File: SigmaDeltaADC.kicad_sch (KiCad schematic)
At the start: 6 parts, among them U5 ADS122C04IPWR

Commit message: Routed most PCB traces
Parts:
- C10, C11: value C -> 0.1u
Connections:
- net 3.3V renamed +3V3
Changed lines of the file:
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@@
     )
   )
-  (symbol (lib_id "SparkFun-PowerSymbols:3.3V") (at 86.868 98.044 0) (unit 1)
-    (in_bom yes) (on_board yes) (fields_autoplaced)
-    (property "Reference" "#SUPPLY01" (id 0) (at 88.138 98.044 0)
-      (effects (font (size 1.143 1.143)) (justify left bottom) hide)
-    )
-    (property "Value" "3.3V" (id 1) (at 88.2651 95.8998 0)
-      (effects (font (size 1.143 1.143)) (justify left))
-    )
-    (property "Footprint" "XXX-00000" (id 2) (at 88.2651 98.8007 0)
-      (effects (font (size 1.524 1.524)) (justify left))
+  (symbol (lib_id "power:+3V3") (at 86.868 98.044 0) (unit 1)
+    (in_bom yes) (on_board yes) (fields_autoplaced)
+    (property "Reference" "#PWR0133" (id 0) (at 86.868 101.854 0)
+      (effects (font (size 1.27 1.27)) hide)
+    )
+    (property "Value" "+3V3" (id 1) (at 86.868 94.4394 0))
+    (property "Footprint" "" (id 2) (at 86.868 98.044 0)
+      (effects (font (size 1.27 1.27)) hide)
     )
     (property "Datasheet" "" (id 3) (at 86.868 98.044 0)
-      (effects (font (size 1.524 1.524)) hide)
-    )
-    (pin "~")
-  )
-  (symbol (lib_id "SparkFun-PowerSymbols:3.3V") (at 113.538 133.096 180) (unit 1)
-    (in_bom yes) (on_board yes) (fields_autoplaced)
-    (property "Reference" "#SUPPLY02" (id 0) (at 112.268 133.096 0)
-      (effects (font (size 1.143 1.143)) (justify left bottom) hide)
-    )
-    (property "Value" "3.3V" (id 1) (at 114.9351 133.1108 0)
-      (effects (font (size 1.143 1.143)) (justify right))
-    )
-    (property "Footprint" "XXX-00000" (id 2) (at 114.9351 136.0117 0)
-      (effects (font (size 1.524 1.524)) (justify right))
+      (effects (font (size 1.27 1.27)) hide)
+    )
+    (pin "1")
+  )
+  (symbol (lib_id "power:+3V3") (at 113.538 133.096 180) (unit 1)
+    (in_bom yes) (on_board yes) (fields_autoplaced)
+    (property "Reference" "#PWR0132" (id 0) (at 113.538 129.286 0)
+      (effects (font (size 1.27 1.27)) hide)
+    )
+    (property "Value" "+3V3" (id 1) (at 114.9351 134.6545 0)
+      (effects (font (size 1.27 1.27)) (justify right))
+    )
+    (property "Footprint" "" (id 2) (at 113.538 133.096 0)
+      (effects (font (size 1.27 1.27)) hide)
     )
     (property "Datasheet" "" (id 3) (at 113.538 133.096 0)
-      (effects (font (size 1.524 1.524)) hide)
-    )
-    (pin "~")
-  )
-  (symbol (lib_id "SparkFun-PowerSymbols:3.3V") (at 115.316 108.204 90) (unit 1)
+      (effects (font (size 1.27 1.27)) hide)
+    )
+    (pin "1")
+  )
+  (symbol (lib_id "power:+3V3") (at 115.316 108.204 90) (unit 1)
     (in_bom yes) (on_board yes)
-    (property "Reference" "#SUPPLY0104" (id 0) (at 115.316 106.934 0)
-      (effects (font (size 1.143 1.143)) (justify left bottom) hide)
-    )
-    (property "Value" "3.3V" (id 1) (at 112.1409 109.2687 90)
-      (effects (font (size 1.143 1.143)) (justify left))
-    )
-    (property "Footprint" "XXX-00000" (id 2) (at 107.5689 108.1458 90)
-      (effects (font (size 1.524 1.524)) (justify left))
+    (property "Reference" "#PWR0134" (id 0) (at 119.126 108.204 0)
+      (effects (font (size 1.27 1.27)) hide)
+    )
+    (property "Value" "+3V3" (id 1) (at 106.4261 108.683 90)
+      (effects (font (size 1.27 1.27)) (justify right))
+    )
+    (property "Footprint" "" (id 2) (at 115.316 108.204 0)
+      (effects (font (size 1.27 1.27)) hide)
     )
     (property "Datasheet" "" (id 3) (at 115.316 108.204 0)
-      (effects (font (size 1.524 1.524)) hide)
-    )
-    (pin "~")
-  )
-  (symbol (lib_id "SparkFun-PowerSymbols:3.3V") (at 156.21 99.822 0) (mirror x) (unit 1)
-    (in_bom yes) (on_board yes)
-    (property "Reference" "#SUPPLY0103" (id 0) (at 157.48 99.822 0)
-      (effects (font (size 1.143 1.143)) (justify left bottom) hide)
-    )
-    (property "Value" "3.3V" (id 1) (at 154.3049 104.0913 0)
-      (effects (font (size 1.143 1.143)) (justify left))
-    )
-    (property "Footprint" "XXX-00000" (id 2) (at 154.5589 106.2302 0)
-      (effects (font (size 1.524 1.524)) (justify left))
+      (effects (font (size 1.27 1.27)) hide)
+    )
+    (pin "1")
+  )
+  (symbol (lib_id "power:+3V3") (at 156.21 99.822 180) (unit 1)
+    (in_bom yes) (on_board yes) (fields_autoplaced)
+    (property "Reference" "#PWR0135" (id 0) (at 156.21 96.012 0)
+      (effects (font (size 1.27 1.27)) hide)
+    )
+    (property "Value" "+3V3" (id 1) (at 157.6071 101.3805 0)
+      (effects (font (size 1.27 1.27)) (justify right))
+    )
+    (property "Footprint" "" (id 2) (at 156.21 99.822 0)
+      (effects (font (size 1.27 1.27)) hide)
     )
     (property "Datasheet" "" (id 3) (at 156.21 99.822 0)
-      (effects (font (size 1.524 1.524)) hide)
-    )
-    (pin "~")
-  )
-  (symbol (lib_id "SparkFun-PowerSymbols:3.3V") (at 169.418 80.264 270) (unit 1)
-    (in_bom yes) (on_board yes)
-    (property "Reference" "#SUPPLY0102" (id 0) (at 169.418 81.534 0)
-      (effects (font (size 1.143 1.143)) (justify left bottom) hide)
-    )
-    (property "Value" "3.3V" (id 1) (at 172.5931 79.1993 90)
-      (effects (font (size 1.143 1.143)) (justify left))
-    )
-    (property "Footprint" "XXX-00000" (id 2) (at 171.8311 77.0202 90)
-      (effects (font (size 1.524 1.524)) (justify left))
+      (effects (font (size 1.27 1.27)) hide)
+    )
+    (pin "1")
+  )
+  (symbol (lib_id "power:+3V3") (at 169.418 80.264 270) (unit 1)
+    (in_bom yes) (on_board yes) (fields_autoplaced)
+    (property "Reference" "#PWR0136" (id 0) (at 165.608 80.264 0)
+      (effects (font (size 1.27 1.27)) hide)
+    )
+    (property "Value" "+3V3" (id 1) (at 172.5931 80.743 90)
+      (effects (font (size 1.27 1.27)) (justify left))
+    )
+    (property "Footprint" "" (id 2) (at 169.418 80.264 0)
+      (effects (font (size 1.27 1.27)) hide)
     )
     (property "Datasheet" "" (id 3) (at 169.418 80.264 0)
-      (effects (font (size 1.524 1.524)) hide)
-    )
-    (pin "~")
-  )
-  (symbol (lib_id "SparkFun-PowerSymbols:3.3V") (at 169.418 82.804 270) (mirror x) (unit 1)
-    (in_bom yes) (on_board yes)
-    (property "Reference" "#SUPPLY0101" (id 0) (at 169.418 81.534 0)
-      (effects (font (size 1.143 1.143)) (justify left bottom) hide)
-    )
-    (property "Value" "3.3V" (id 1) (at 172.5931 83.8687 90)
-      (effects (font (size 1.143 1.143)) (justify left))
-    )
-    (property "Footprint" "XXX-00000" (id 2) (at 172.3391 81.7298 90)
-      (effects (font (size 1.524 1.524)) (justify left))
+      (effects (font (size 1.27 1.27)) hide)
+    )
+    (pin "1")
+  )
+  (symbol (lib_id "power:+3V3") (at 169.418 82.804 270) (unit 1)
+    (in_bom yes) (on_board yes) (fields_autoplaced)
+    (property "Reference" "#PWR0137" (id 0) (at 165.608 82.804 0)
+      (effects (font (size 1.27 1.27)) hide)
+    )
+    (property "Value" "+3V3" (id 1) (at 172.5931 83.283 90)
+      (effects (font (size 1.27 1.27)) (justify left))
+    )
+    (property "Footprint" "" (id 2) (at 169.418 82.804 0)
+      (effects (font (size 1.27 1.27)) hide)
     )
     (property "Datasheet" "" (id 3) (at 169.418 82.804 0)
-      (effects (font (size 1.524 1.524)) hide)
-    )
-    (pin "~")
+      (effects (font (size 1.27 1.27)) hide)
+    )
+    (pin "1")
   )
   (symbol (lib_id "power:GNDD") (at 117.602 89.408 270) (unit 1)
@@
       (effects (font (size 1.27 1.27)) (justify left))
     )
-    (property "Value" "C" (id 1) (at 164.7191 76.5426 0)
+    (property "Value" "0.1u" (id 1) (at 164.7191 76.5426 0)
       (effects (font (size 1.27 1.27)) (justify left))
     )
@@
       (effects (font (size 1.27 1.27)) (justify left))
     )
-    (property "Value" "C" (id 1) (at 171.3231 86.5254 0)
-      (effects (font (size 1.27 1.27)) (justify left))
-    )
+    (property "Value" "0.1u" (id 1) (at 171.3231 86.5254 0)
+      (effects (font (size 1.27 1.27)) (justify left))
+    )

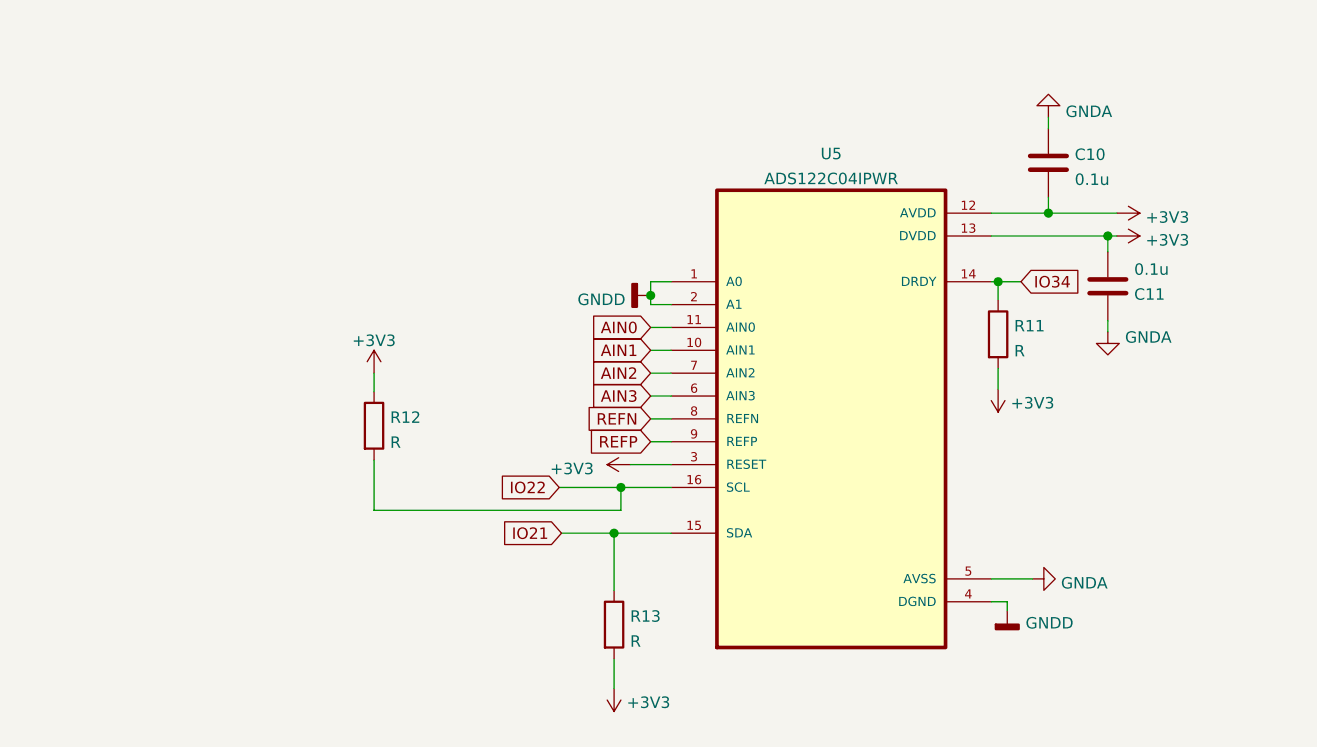
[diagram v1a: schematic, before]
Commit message: Added VOC and Optical Sensors
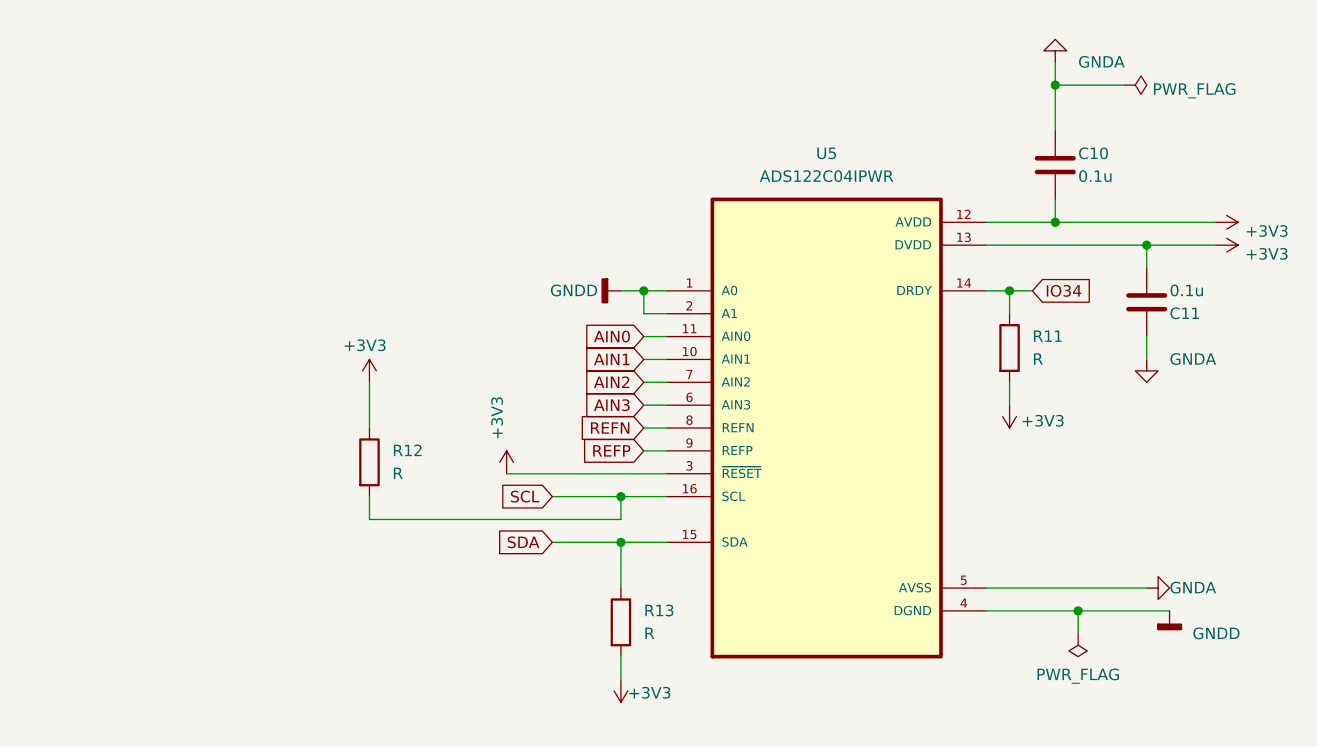
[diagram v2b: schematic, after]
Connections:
- net IO21 renamed SDA
- net IO22 renamed SCL
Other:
- moved on the sheet: C10, C11, R11, R12, R13, U5

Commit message: Vertical Horizontal Traces
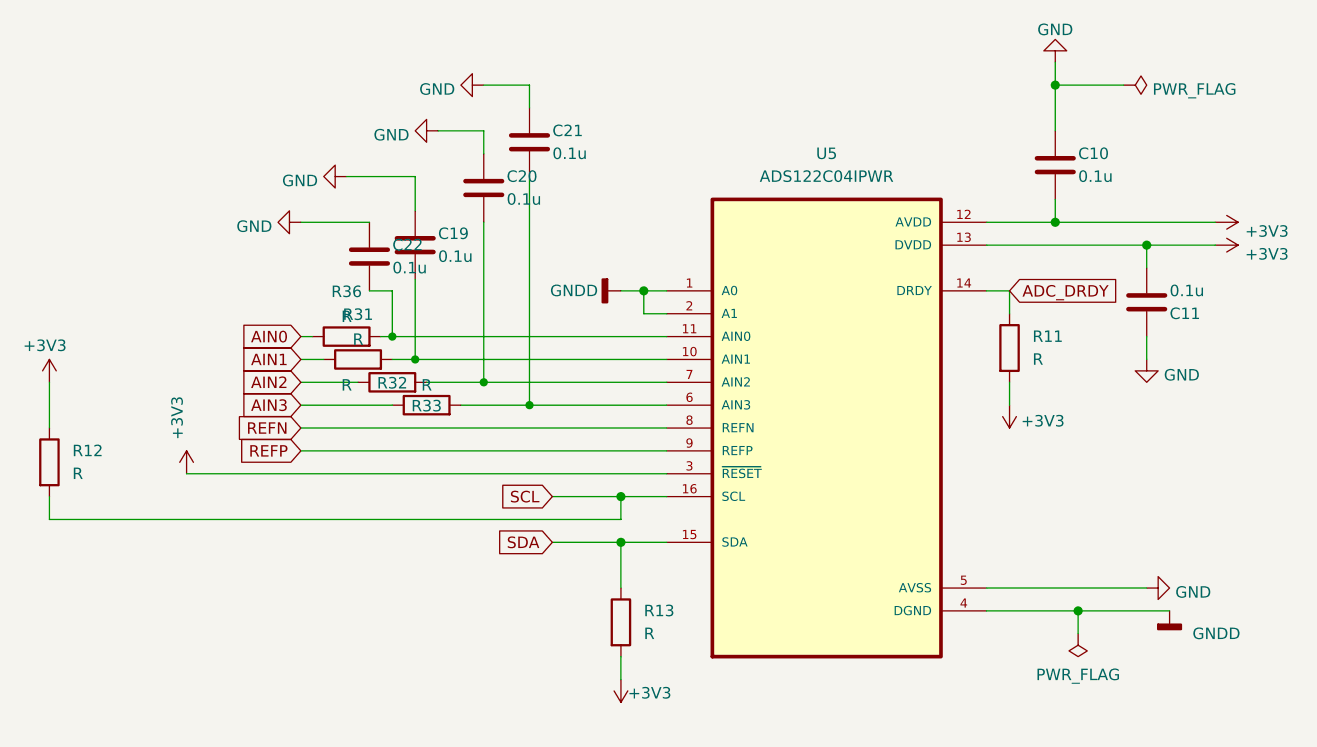
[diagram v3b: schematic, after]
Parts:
- added C19, C20, C21, C22: 0.1u, Capacitor_SMD:C_0603_1608Metric, symbol Device:C
- added R31, R32, R33, R36: R, Resistor_SMD:R_0603_1608Metric_Pad0.98x0.95mm_HandSolder, symbol Device:R
- U5: footprint ADC:SOP65P640X120-16N -> ADS122C04IPWR:SOP65P640X120-16N
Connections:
- net AIN0: now also R36.1; no longer U5.11 (AIN0)
- net AIN1: now also R31.1; no longer U5.10 (AIN1)
- net AIN2: now also R32.1; no longer U5.7 (AIN2)
- net AIN3: now also R33.1; no longer U5.6 (AIN3)
- net GNDA renamed GND
- net GND: now also C19.1, C20.1, C21.1, C22.1
- net IO34 renamed ADC_DRDY
- new net: C19.2, R31.2, U5.10 (AIN1)
- new net: C22.2, R36.2, U5.11 (AIN0)
- new net: C21.2, R33.2, U5.6 (AIN3)
- new net: C20.2, R32.2, U5.7 (AIN2)
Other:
- moved on the sheet: R12
